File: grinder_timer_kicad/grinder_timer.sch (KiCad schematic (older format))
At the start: 24 parts, among them IC1 ATMEGA328P-P, U1 SSD1306_128x64OLED, U2 serial_to_usb

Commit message: Worked on the schematic and footprints.
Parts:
- removed REG1: LM7805, TO_SOT_Packages_THT:TO-220_Neutral123_Vertical, symbol LM7805
- removed SW_RST1: SW_Push_Dual, Buttons_Switches_THT:SW_PUSH_6mm, symbol SW_Push_Dual
- added HA1_BUTTONS1, HB1_BUTTONS1: CONN_01X04, Pin_Headers:Pin_Header_Straight_1x04, symbol CONN_01X04
- added HA2_OLED1, HB2_OLED1: CONN_01X05, Pin_Headers:Pin_Header_Straight_1x05, symbol CONN_01X05
- added RESET1: SW_Push, Buttons_Switches_THT:SW_PUSH_6mm, symbol SW_Push
- added T1: TRANS, grinder_timer:TRANS, symbol TRANS
- added U3: LM7805CT, TO-220, symbol LM7805CT
- Active1, Motor1, Neutral1: footprint (none) -> grinder_timer:SPADE_LUG
- D_RECT1: footprint (none) -> grinder_timer:BRIDGE_RECT
- RELAY1: footprint grinder_timer:Relay -> grinder_timer:RELAY
- R_RST1, R_SCL1, R_SDA1: footprint (none) -> Resistors_THT:Resistor_Horizontal_RM10mm
- SW_DOWN1, SW_LEFT1, SW_RIGHT1, SW_UP1: footprint Buttons_Switches_THT:SW_PUSH_6mm -> grinder_timer:TACT
- U1: footprint (none) -> grinder_timer:OLED
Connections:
- net +5V: now also BUTTON_GRIND1.4 (A), HA2_OLED1.4 (P4), U3.3 (OUT); no longer BUTTON_GRIND1.3 (K), U1.7 (Vin)
- net GND: now also BUTTON_GRIND1.3 (K), HA2_OLED1.5 (P5), RESET1.2, U3.2 (GND); no longer BUTTON_GRIND1.4 (A), SW_DOWN1.1, SW_LEFT1.1, SW_RIGHT1.1, SW_UP1.1, U1.3 (SA0), U1.5 ((NC)), U1.8 (GND)
- net at SW_DOWN1.3: now also SW_DOWN1.1, HB1_BUTTONS1.2 (P2)
- net GNDD: now reaches SW_DOWN1.4
- net GNDD: now also SW_DOWN1.2, SW_LEFT1.2, SW_LEFT1.4, SW_RIGHT1.2, SW_RIGHT1.4, SW_UP1.2, SW_UP1.4, U1.3 (SA0), U1.5 ((NC)), U1.8 (GND), HB2_OLED1.5 (P5)
- net at SW_UP1.3: now also SW_UP1.1, HB1_BUTTONS1.1 (P1)
- net at SW_LEFT1.3: now also SW_LEFT1.1, HB1_BUTTONS1.3 (P3)
- net at SW_RIGHT1.3: now also SW_RIGHT1.1, HB1_BUTTONS1.4 (P4)
- net at Neutral1.1, RELAY1.11: now also T1.1 (PF); no longer D_RECT1.4
- net at C1.1, C2.1, D_RECT1.1 (+): now also U3.1 (IN)
- net at D_RECT1.3: now also T1.6 (S1_1), T1.9 (S2_1); no longer Active1.1
- net BUTTON_DOWN renamed HA1_BUTTON_DOWN
- net HA1_BUTTON_DOWN: now also HA1_BUTTONS1.2 (P2); no longer SW_DOWN1.2
- net BUTTON_LEFT renamed HA1_BUTTON_LEFT
- net HA1_BUTTON_LEFT: now also HA1_BUTTONS1.3 (P3); no longer SW_LEFT1.2
- net BUTTON_RIGHT renamed HA1_BUTTON_RIGHT
- net HA1_BUTTON_RIGHT: now also HA1_BUTTONS1.4 (P4); no longer SW_RIGHT1.2
- net BUTTON_UP renamed HA1_BUTTON_UP
- net HA1_BUTTON_UP: now also HA1_BUTTONS1.1 (P1); no longer SW_UP1.2
- net RESET renamed HA2_RESET
- net HA2_RESET: now also HA2_OLED1.2 (P2), RESET1.1; no longer U1.4 (RST)
- net SCL renamed HA2_SCL
- net HA2_SCL: now also HA2_OLED1.3 (P3); no longer U1.2 (SCL)
- net SDA renamed HA2_SDA
- net HA2_SDA: now also HA2_OLED1.1 (P1); no longer U1.1 (SDA)
- new net: D_RECT1.4, T1.10 (S2_2), T1.7 (S1_2)
- new net: Active1.1, T1.5 (P1)
- new net +5VD: HB2_OLED1.4 (P4), U1.7 (Vin)
- new net HB2_RESET: HB2_OLED1.3 (P3), U1.4 (RST)
- new net HB2_SCL: HB2_OLED1.2 (P2), U1.2 (SCL)
- new net HB2_SDA: HB2_OLED1.1 (P1), U1.1 (SDA)
- no-connect marks 21 -> 14
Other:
- note added: "A"
- note added: "B"
- moved on the sheet: Active1, BUTTON_GRIND1, C1, C2, C3, C4, CON_ISP1, D_RECT1, IC1, Neutral1, RELAY1, RTC_Crystal1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

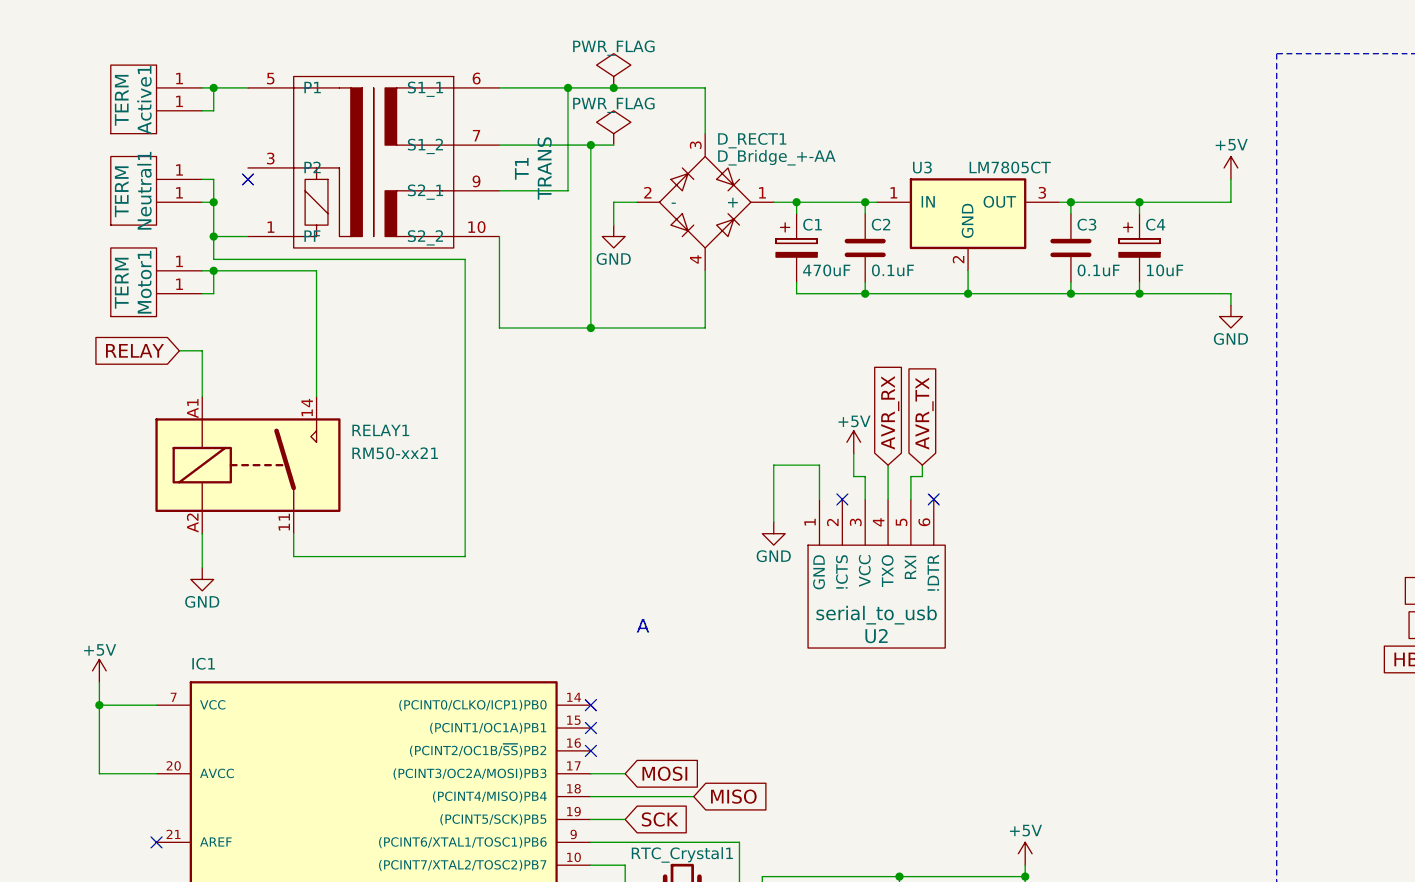
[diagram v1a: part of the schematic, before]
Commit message: Work on the schematic.  Began PCB layout.
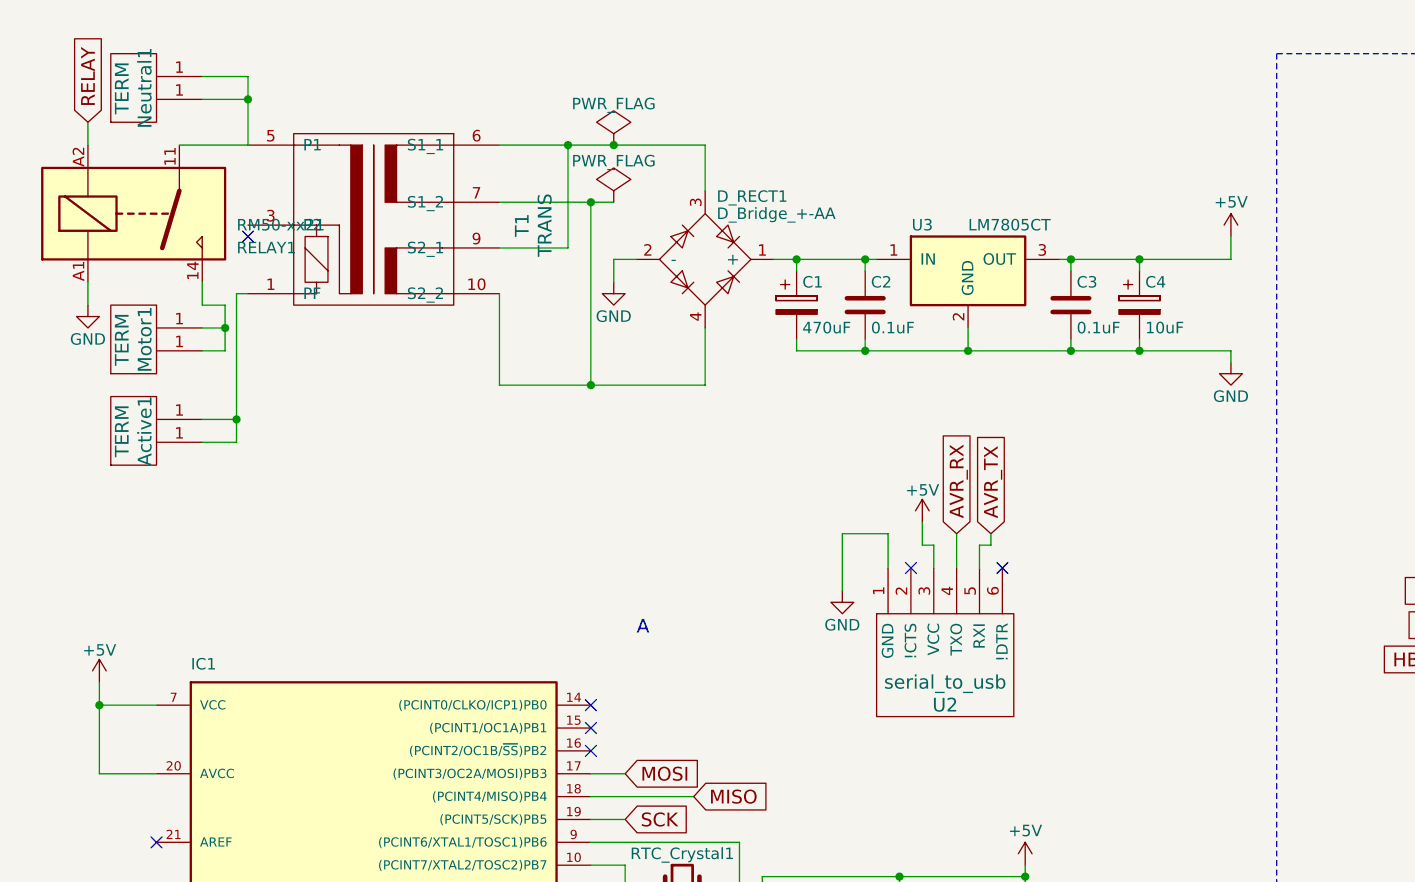
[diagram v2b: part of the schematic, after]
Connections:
- net GND: now also RELAY1.A1; no longer RELAY1.A2
- net RELAY: now also RELAY1.A2; no longer RELAY1.A1
- net at Neutral1.1, RELAY1.11: now also T1.5 (P1); no longer T1.1 (PF)
- net at Active1.1: now also T1.1 (PF); no longer T1.5 (P1)
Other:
- moved on the sheet: Active1, C1, C2, C3, C4, D_RECT1, Motor1, Neutral1, RELAY1, T1, U2, U3

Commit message: Finished PCB layouts (first rev).
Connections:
- net +5V: no longer R_SCL1.1, R_SDA1.1
- net +5VD: now also R_SCL1.2, R_SDA1.2
- net GNDD: now also HB1_BUTTONS1.1 (P1), SW_UP1.1, SW_UP1.3
- net HA2_SCL: no longer R_SCL1.2
- net HA2_SDA: no longer R_SDA1.2
- net HB2_SCL: now also R_SCL1.1
- net HB2_SDA: now also R_SDA1.1
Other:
- moved on the sheet: HB1_BUTTONS1, RESET1, R_RST1, R_SCL1, R_SDA1, SW_DOWN1, SW_LEFT1, SW_RIGHT1, SW_UP1

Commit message: Fixed a mis-wired push button on the schematic and PCB layout.
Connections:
- net GNDD: no longer HB1_BUTTONS1.1 (P1), SW_UP1.1, SW_UP1.3
- new net: HB1_BUTTONS1.1 (P1), SW_UP1.1, SW_UP1.3
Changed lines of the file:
@@
 Wire Wire Line
 	9800 1000 9700 1000
-Wire Wire Line
-	10100 2050 10100 2400
 Connection ~ 10100 2050
 Wire Wire Line
@@
 	10950 700  10950 2450
 Wire Wire Line
-	10100 2400 10950 2400
-Connection ~ 10950 2400
-Wire Wire Line
 	9700 700  10200 700
 Wire Wire Line
@@
 	3250 4650 3000 4650
 Wire Wire Line
-	10200 2250 10100 2250
-Connection ~ 10100 2250
-Wire Wire Line
 	10600 2250 10950 2250
 Connection ~ 10950 2250
+Wire Wire Line
+	10200 2250 10100 2250
+Wire Wire Line
+	10100 2250 10100 2050
 $EndSCHEMATC

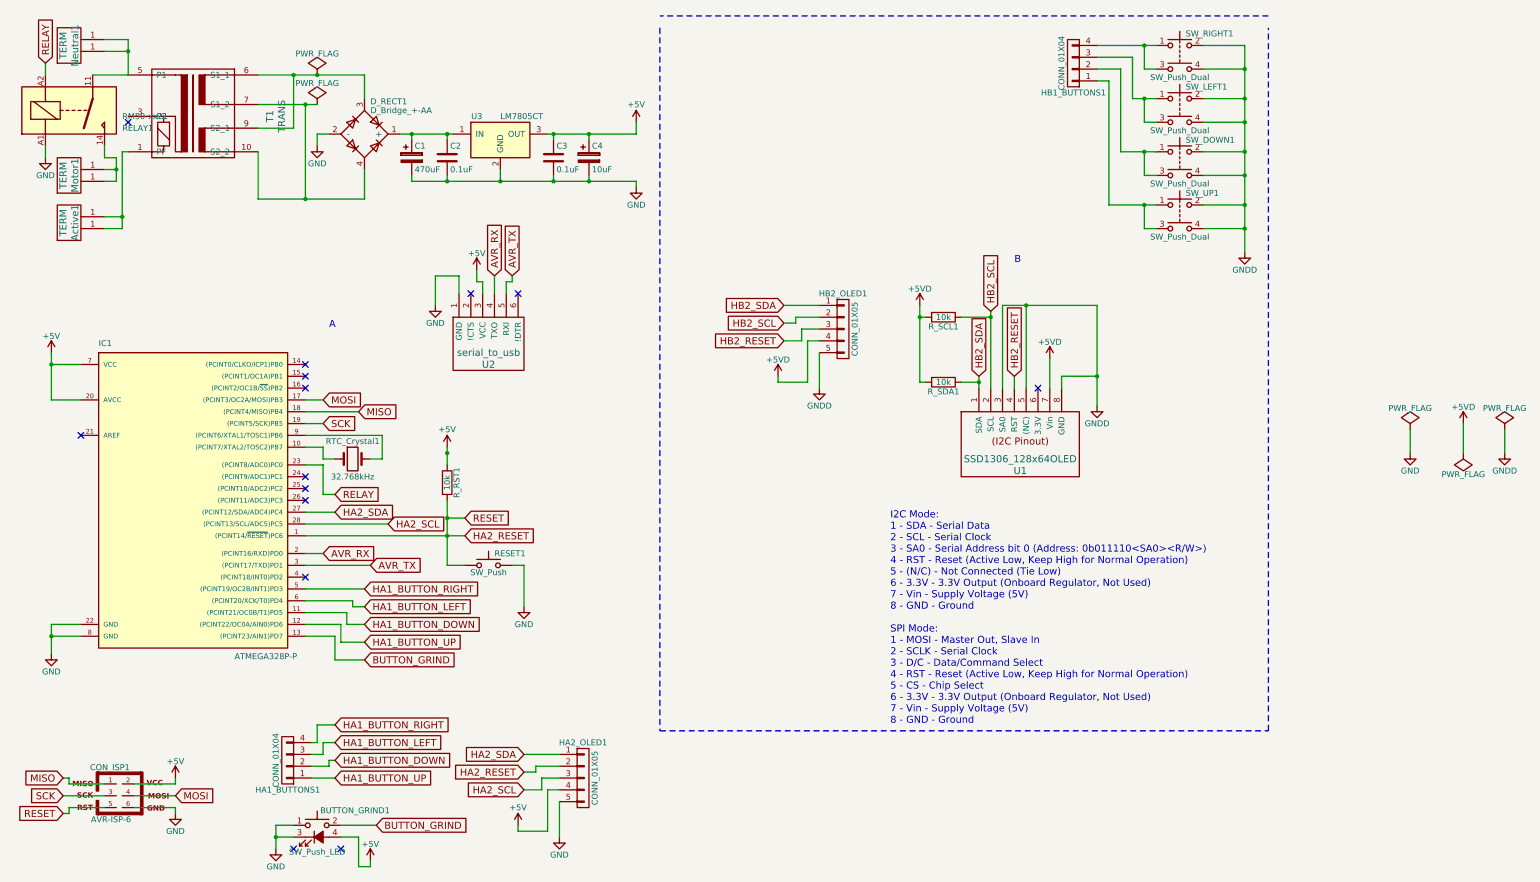
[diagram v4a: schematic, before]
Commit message: First prototype PCB fabricated and somewhat successful.  Major revision to improve.
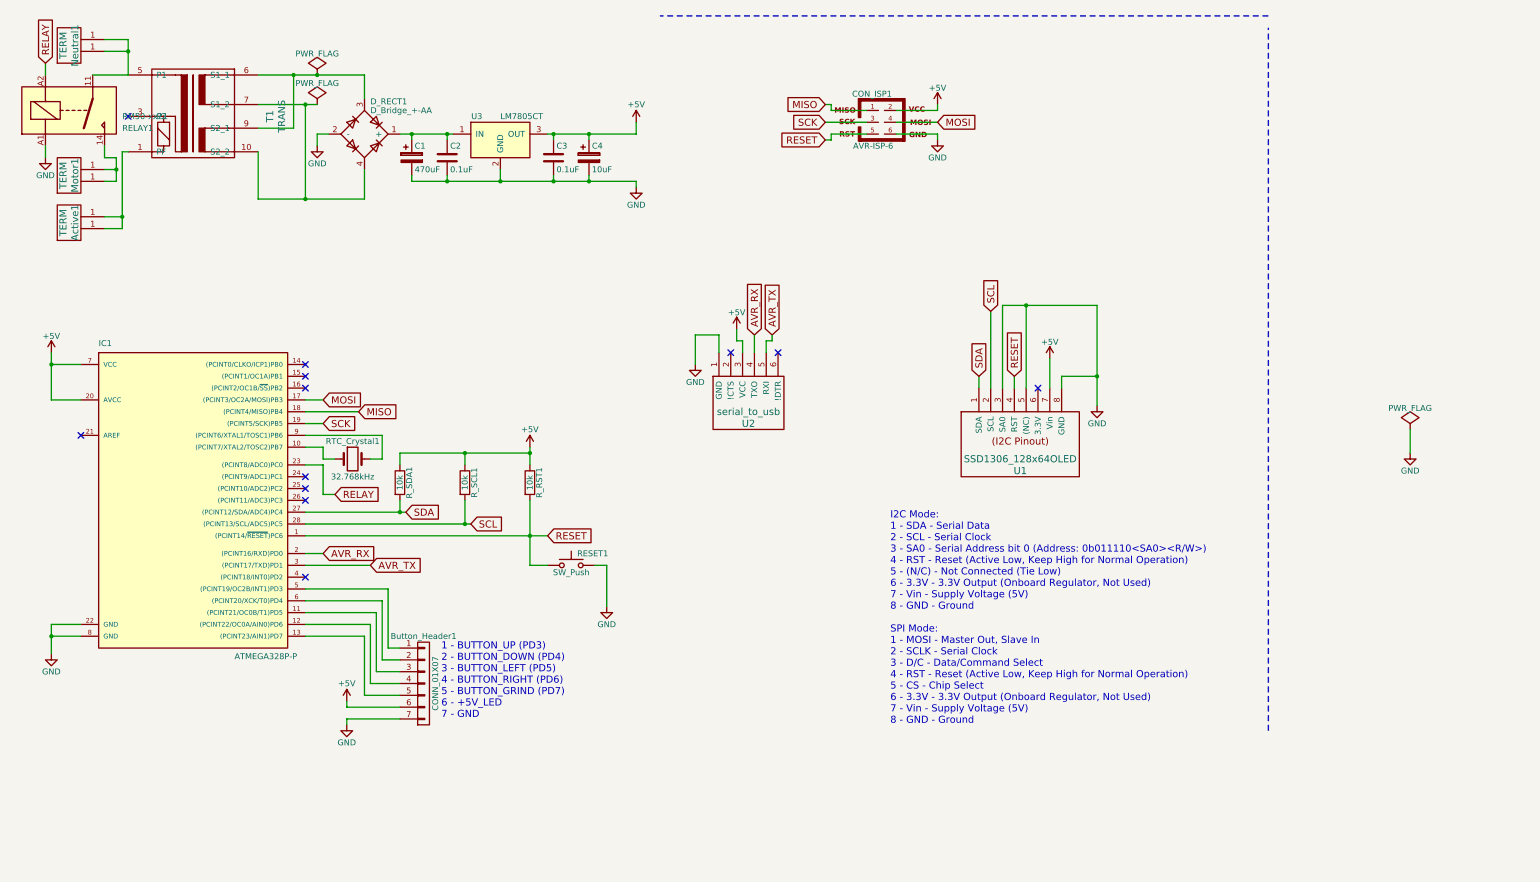
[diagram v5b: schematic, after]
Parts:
- removed BUTTON_GRIND1: SW_Push_LED, Pin_Headers:Pin_Header_Straight_1x04, symbol SW_Push_LED
- removed HA1_BUTTONS1, HB1_BUTTONS1: CONN_01X04, Pin_Headers:Pin_Header_Straight_1x04, symbol CONN_01X04
- removed HA2_OLED1, HB2_OLED1: CONN_01X05, Pin_Headers:Pin_Header_Straight_1x05, symbol CONN_01X05
- removed SW_DOWN1, SW_LEFT1, SW_RIGHT1, SW_UP1: SW_Push_Dual, grinder_timer:TACT, symbol SW_Push_Dual
- added Button_Header1: CONN_01X07, Pin_Headers:Pin_Header_Straight_1x07, symbol CONN_01X07
- U1: footprint grinder_timer:OLED -> Pin_Headers:Pin_Header_Straight_1x08
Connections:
- net GNDD is gone; now on net GND: U1.3 (SA0), U1.5 ((NC)), U1.8 (GND)
- net HB2_RESET is gone; now on net RESET: U1.4 (RST)
- net +5V: now also R_SCL1.1, R_SDA1.1, U1.7 (Vin), Button_Header1.6 (P6)
- net GND: now also Button_Header1.7 (P7)
- removed net +5VD: R_SCL1.2, R_SDA1.2, U1.7 (Vin)
- net BUTTON_GRIND: no longer names the net of IC1.13 ((PCINT23/AIN1)PD7)
- net BUTTON_GRIND: now also Button_Header1.5 (P5)
- net HA1_BUTTON_DOWN: no longer names the net of IC1.11 ((PCINT21/OC0B/T1)PD5)
- net HA1_BUTTON_DOWN: now also Button_Header1.3 (P3)
- net HA1_BUTTON_LEFT: no longer names the net of IC1.6 ((PCINT20/XCK/T0)PD4)
- net HA1_BUTTON_LEFT: now also Button_Header1.2 (P2)
- net HA1_BUTTON_RIGHT: no longer names the net of IC1.5 ((PCINT19/OC2B/INT1)PD3)
- net HA1_BUTTON_RIGHT: now also Button_Header1.1 (P1)
- net HA1_BUTTON_UP: no longer names the net of IC1.12 ((PCINT22/OC0A/AIN0)PD6)
- net HA1_BUTTON_UP: now also Button_Header1.4 (P4)
- net HA2_RESET renamed RESET
- net HA2_SCL renamed SCL
- net SCL: now also R_SCL1.2, U1.2 (SCL)
- net HA2_SDA renamed SDA
- net SDA: now also R_SDA1.2, U1.1 (SDA)
- removed net HB2_SCL: R_SCL1.1, U1.2 (SCL)
- removed net HB2_SDA: R_SDA1.1, U1.1 (SDA)
- no-connect marks 14 -> 12
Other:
- note added: "1 - BUTTON_UP (PD3)\n2 - BUTTON_DOWN (PD4)\n3 - BUTTON_LEFT (PD5)\n4 - BUTTON_RIGHT (PD6)\n5 - BUTTON_GRIND (PD7)\n6 - +5V_LED\n7 - GND"
- note removed: "A"
- note removed: "B"
- moved on the sheet: CON_ISP1, RESET1, R_RST1, R_SCL1, R_SDA1, U2
